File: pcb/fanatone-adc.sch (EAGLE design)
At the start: 43 parts, among them IC2 DIT4192-H, IC3 PCM4201-TSSOP-16, Q1 SST5484, U1 OPA1612AID, U2 TPS62240DRVTG4

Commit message: add datasheets, remove capacitor over R6 at booster
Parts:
- removed C21: 4.7pF, rcl:C-EUC0603
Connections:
- removed net 4V: C10.1, C3.1
- new net 5V: C11.2, C12.2, IC3.VCC
- new net N$12: IC2.SCLK, IC3.BCK
- new net N$14: IC2.SYNC, IC3.FSYNC
- new net N$15: IC2.SDATA, IC3.DATA
- new net N$17: IC2.MCLK, IC3.SCKI
- net 3V3: now also IC3.VDD
- net GND: now also C10.1, C3.1, IC3.DGND, IC3.RATE, IC3.S/M, IC3.VREF-; no longer C10.2, C3.2
- net N$5: now also C10.2, C3.2, IC3.VREF+; no longer C11.2, C12.2
- net N$7: no longer C21.2
- net VCAPSULE: no longer C21.1
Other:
- note added: "24.576 MHz"
- note added: "RATE pin level LOW - high performance, double speed, 96kHz HIGH - low power, 48kHz FLOAT - high performance, 48 kHz"
- note added: "VDPP input 9.5...12.5V"
- note added: "differential input max 5Vp-p 15k input impedance per pin"
- note added: "set R5, R6 for output voltage VCAPSULE = 48V"
- moved on the sheet: C10, C11, C12, C13, C14, C3, C6, C7, C8, D1, R1

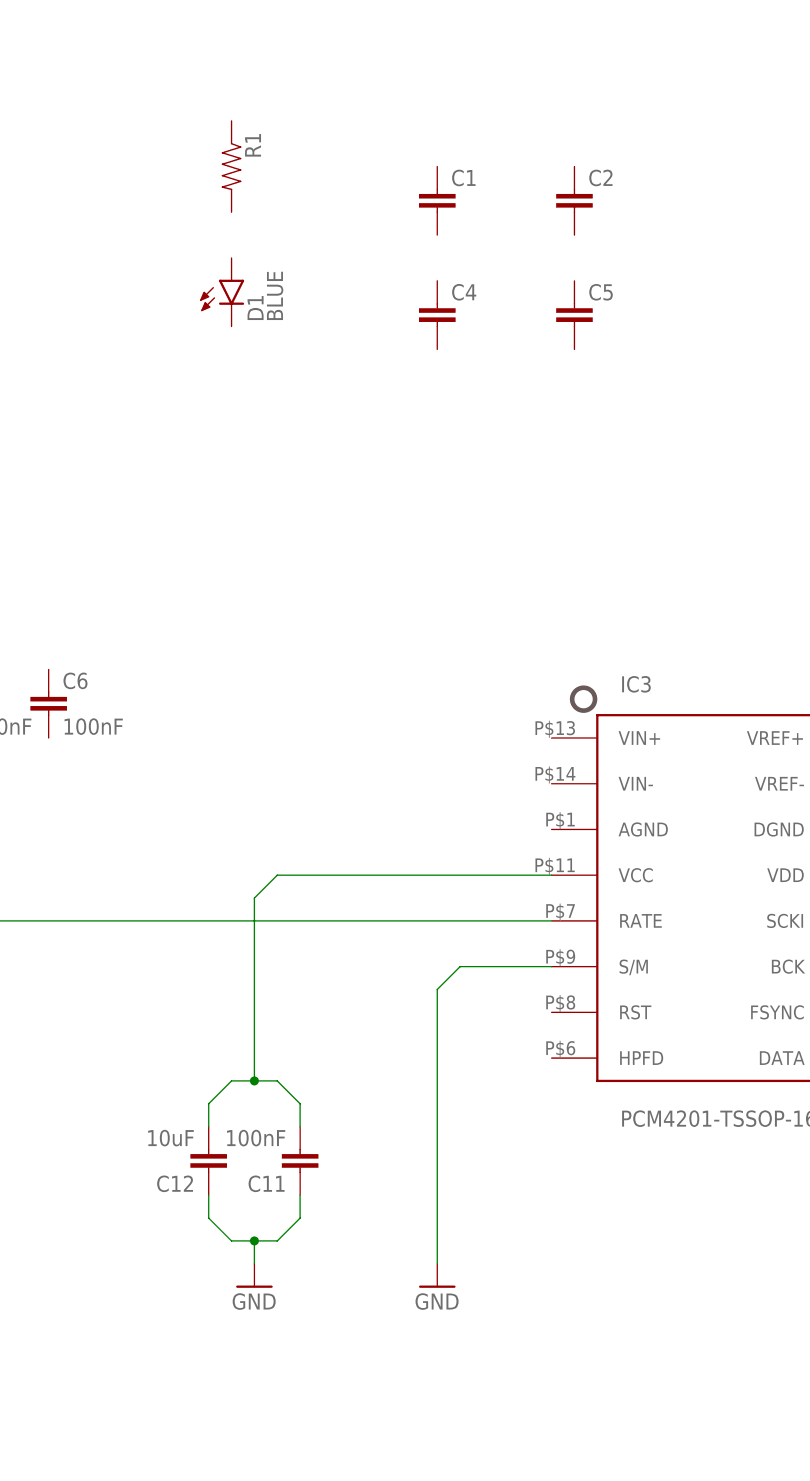
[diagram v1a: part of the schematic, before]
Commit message: Rectangular FAT Capsule R design
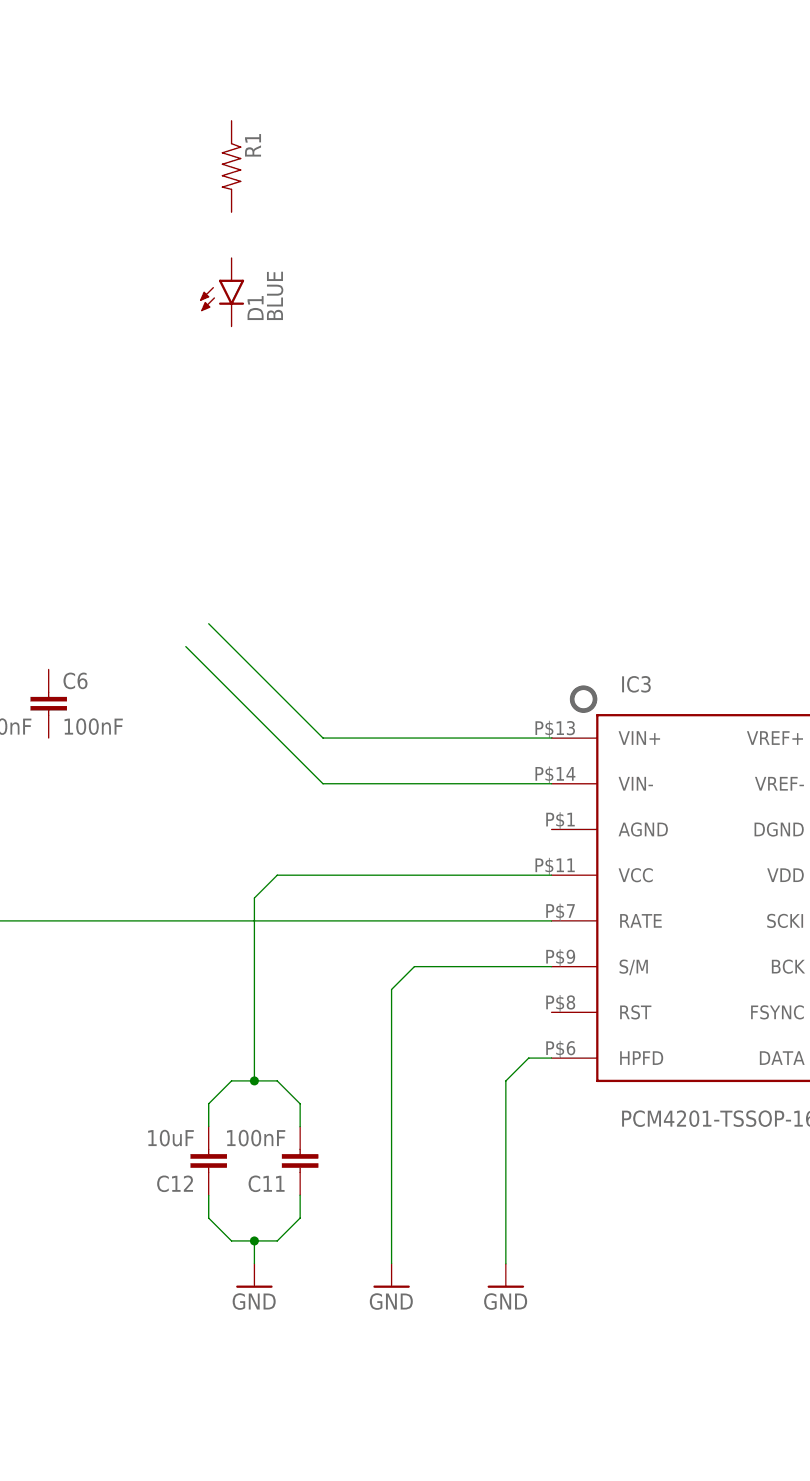
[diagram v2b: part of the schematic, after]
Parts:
- removed C1: (no value), rcl:C-EUC0402K
- removed C2: (no value), rcl:C-EUC0805
- removed C4: (no value), SparkFun-Passives:CAP0603-CAP
- removed C5: (no value), SparkFun-Passives:CAP0805
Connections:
- new net N$19: IC3.VIN+
- new net N$20: IC3.VIN-
- net GND: now also IC3.HPFD
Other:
- note added: "HPFD LOW - enable high pass at 2Hz (-3dB) HIGH - disable (no DC decoupling)"
- note added: "S/M LOW - master"
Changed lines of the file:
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@@
 <part name="FRAME1" library="frames" deviceset="A3L-LOC" device=""/>
 <part name="FRAME2" library="frames" deviceset="A3L-LOC" device=""/>
-<part name="C1" library="rcl" deviceset="C-EU" device="C0402K"/>
-<part name="C2" library="rcl" deviceset="C-EU" device="C0805"/>
 <part name="IC2" library="texas" deviceset="DIT4192-H" device=""/>
 <part name="U$1" library="SparkFun-FreqCtrl" deviceset="CRYSTAL-GROUNDED" device=""/>
-<part name="C4" library="SparkFun-Passives" deviceset="CAP" device="0603-CAP"/>
-<part name="C5" library="SparkFun-Passives" deviceset="CAP" device="0805"/>
 <part name="R1" library="SparkFun-Passives" deviceset="RESISTOR" device="0603-RES"/>
 <part name="D1" library="SparkFun-LED" deviceset="LED-BLUE" device="0603" value="BLUE"/>
@@
 <part name="GND2" library="SparkFun-Aesthetics" deviceset="GND" device=""/>
 <part name="GND16" library="SparkFun-Aesthetics" deviceset="GND" device=""/>
+<part name="GND17" library="SparkFun-Aesthetics" deviceset="GND" device=""/>
 </parts>
 <sheets>
@@
 <text x="312.42" y="142.24" size="1.778" layer="91">9.5 ... 12.5V - Vdrop_D3
 max. 250mA</text>
-<text x="81.28" y="132.08" size="1.778" layer="98">differential input
+<text x="58.42" y="134.62" size="1.778" layer="98">differential input
 max 5Vp-p
 15k input impedance per pin</text>
@@
 <text x="154.94" y="-185.42" size="1.778" layer="98">set R5, R6 for output voltage
 VCAPSULE = 48V</text>
+<text x="81.28" y="66.04" size="1.778" layer="98">HPFD
+LOW - enable high pass at 2Hz (-3dB)
+HIGH - disable (no DC decoupling)</text>
+<text x="65.278" y="66.548" size="1.778" layer="98" rot="R90">S/M
+LOW - master</text>
 </plain>
 <instances>
@@
 <instance part="FRAME1" gate="G$1" x="-7.62" y="-10.16"/>
 <instance part="FRAME2" gate="G$1" x="419.1" y="-10.16"/>
-<instance part="C1" gate="G$1" x="71.12" y="185.42"/>
-<instance part="C2" gate="G$1" x="86.36" y="185.42"/>
 <instance part="IC2" gate="G$1" x="238.76" y="106.68"/>
 <instance part="U$1" gate="G$1" x="190.5" y="182.88"/>
-<instance part="C4" gate="G$1" x="71.12" y="170.18"/>
-<instance part="C5" gate="G$1" x="86.36" y="170.18"/>
 <instance part="R1" gate="G$1" x="48.26" y="187.96" rot="R270"/>
 <instance part="D1" gate="G$1" x="48.26" y="175.26"/>
@@
 <instance part="U1" gate="A" x="604.52" y="193.04"/>
 <instance part="IC3" gate="G$1" x="101.6" y="106.68"/>
-<instance part="GND14" gate="1" x="71.12" y="63.5"/>
+<instance part="GND14" gate="1" x="66.04" y="63.5"/>
 <instance part="GND15" gate="1" x="50.8" y="63.5"/>
 <instance part="C3" gate="G$1" x="187.96" y="78.74" rot="R180"/>
@@
 <instance part="GND2" gate="1" x="182.88" y="63.5"/>
 <instance part="GND16" gate="1" x="7.62" y="63.5"/>
+<instance part="GND17" gate="1" x="78.74" y="63.5"/>
 </instances>
 <busses>
@@
 <segment>
 <pinref part="IC3" gate="G$1" pin="S/M"/>
-<wire x1="83.82" y1="99.06" x2="73.66" y2="99.06" width="0.1524" layer="91"/>
-<wire x1="73.66" y1="99.06" x2="71.12" y2="96.52" width="0.1524" layer="91"/>
-<wire x1="71.12" y1="96.52" x2="71.12" y2="66.04" width="0.1524" layer="91"/>
+<wire x1="83.82" y1="99.06" x2="68.58" y2="99.06" width="0.1524" layer="91"/>
+<wire x1="68.58" y1="99.06" x2="66.04" y2="96.52" width="0.1524" layer="91"/>
+<wire x1="66.04" y1="96.52" x2="66.04" y2="66.04" width="0.1524" layer="91"/>
 <pinref part="GND14" gate="1" pin="GND"/>
 </segment>
@@
 <wire x1="5.08" y1="119.38" x2="2.54" y2="116.84" width="0.1524" layer="91"/>
 <wire x1="2.54" y1="106.68" x2="2.54" y2="116.84" width="0.1524" layer="91"/>
+</segment>
+<segment>
+<pinref part="IC3" gate="G$1" pin="HPFD"/>
+<wire x1="83.82" y1="88.9" x2="81.28" y2="88.9" width="0.1524" layer="91"/>
+<wire x1="81.28" y1="88.9" x2="78.74" y2="86.36" width="0.1524" layer="91"/>
+<wire x1="78.74" y1="86.36" x2="78.74" y2="66.04" width="0.1524" layer="91"/>
+<pinref part="GND17" gate="1" pin="GND"/>
 </segment>
 </net>
@@
 </segment>
 </net>
+<net name="N$19" class="0">
+<segment>
+<pinref part="IC3" gate="G$1" pin="VIN+"/>
+<wire x1="83.82" y1="124.46" x2="58.42" y2="124.46" width="0.1524" layer="91"/>
+<wire x1="58.42" y1="124.46" x2="45.72" y2="137.16" width="0.1524" layer="91"/>
+</segment>
+</net>
+<net name="N$20" class="0">
+<segment>
+<pinref part="IC3" gate="G$1" pin="VIN-"/>
+<wire x1="83.82" y1="119.38" x2="58.42" y2="119.38" width="0.1524" layer="91"/>
+<wire x1="58.42" y1="119.38" x2="43.18" y2="134.62" width="0.1524" layer="91"/>
+</segment>
+</net>

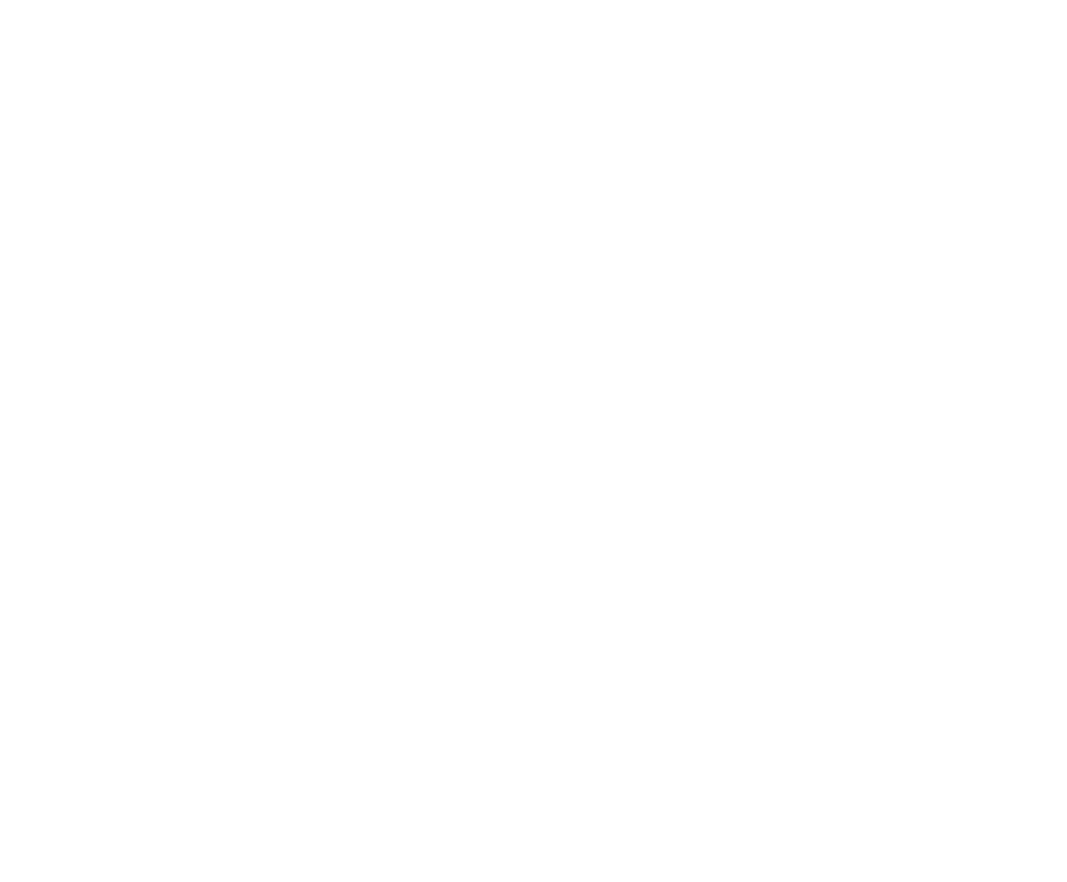
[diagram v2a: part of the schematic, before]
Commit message: start with OPA2134 at the initial gain stage
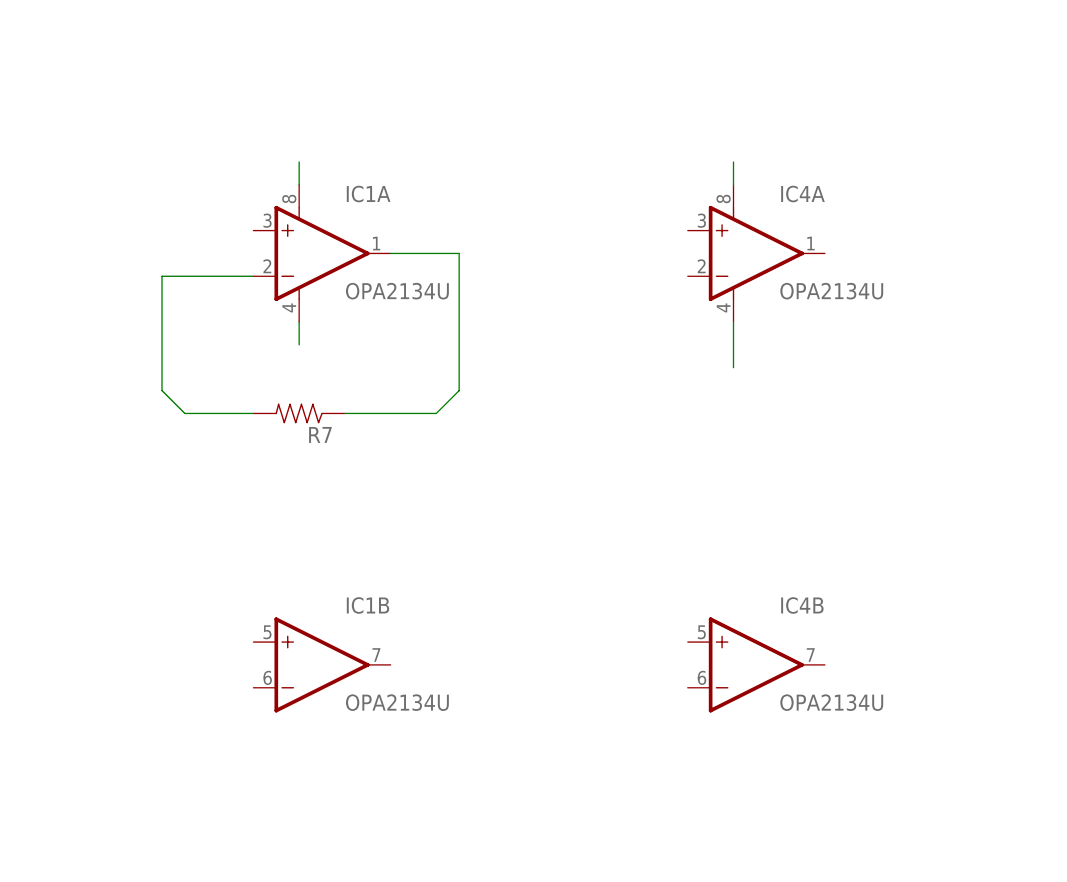
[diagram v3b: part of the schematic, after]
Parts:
- added IC1, IC4: OPA2134U, burr-brown:OPA2134U
- added R7: (no value), SparkFun-Passives:RESISTOR0603-RES
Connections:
- new net N$21: IC1A.OUT, R7.1
- new net N$22: IC1A.-IN, R7.2
- new net N$23: IC1A.V-
- new net N$24: IC1A.V+
- new net N$25: IC4A.V+
- new net N$26: IC4A.V-
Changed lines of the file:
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@@
 <part name="GND16" library="SparkFun-Aesthetics" deviceset="GND" device=""/>
 <part name="GND17" library="SparkFun-Aesthetics" deviceset="GND" device=""/>
+<part name="IC1" library="burr-brown" deviceset="OPA2134" device="U"/>
+<part name="IC4" library="burr-brown" deviceset="OPA2134" device="U"/>
+<part name="R7" library="SparkFun-Passives" deviceset="RESISTOR" device="0603-RES"/>
 </parts>
 <sheets>
@@
 <instance part="GND16" gate="1" x="7.62" y="63.5"/>
 <instance part="GND17" gate="1" x="78.74" y="63.5"/>
+<instance part="IC1" gate="A" x="510.54" y="96.52"/>
+<instance part="IC1" gate="B" x="510.54" y="50.8"/>
+<instance part="IC4" gate="A" x="558.8" y="96.52"/>
+<instance part="IC4" gate="B" x="558.8" y="50.8"/>
+<instance part="R7" gate="G$1" x="508" y="78.74" rot="R180"/>
 </instances>
 <busses>
@@
 </segment>
 </net>
+<net name="N$21" class="0">
+<segment>
+<pinref part="R7" gate="G$1" pin="1"/>
+<wire x1="513.08" y1="78.74" x2="523.24" y2="78.74" width="0.1524" layer="91"/>
+<wire x1="523.24" y1="78.74" x2="525.78" y2="81.28" width="0.1524" layer="91"/>
+<wire x1="525.78" y1="81.28" x2="525.78" y2="96.52" width="0.1524" layer="91"/>
+<pinref part="IC1" gate="A" pin="OUT"/>
+<wire x1="525.78" y1="96.52" x2="518.16" y2="96.52" width="0.1524" layer="91"/>
+</segment>
+</net>
+<net name="N$22" class="0">
+<segment>
+<pinref part="IC1" gate="A" pin="-IN"/>
+<wire x1="502.92" y1="93.98" x2="492.76" y2="93.98" width="0.1524" layer="91"/>
+<wire x1="492.76" y1="93.98" x2="492.76" y2="81.28" width="0.1524" layer="91"/>
+<wire x1="492.76" y1="81.28" x2="495.3" y2="78.74" width="0.1524" layer="91"/>
+<pinref part="R7" gate="G$1" pin="2"/>
+<wire x1="495.3" y1="78.74" x2="502.92" y2="78.74" width="0.1524" layer="91"/>
+</segment>
+</net>
+<net name="N$23" class="0">
+<segment>
+<pinref part="IC1" gate="A" pin="V-"/>
+<wire x1="508" y1="88.9" x2="508" y2="86.36" width="0.1524" layer="91"/>
+</segment>
+</net>
+<net name="N$24" class="0">
+<segment>
+<pinref part="IC1" gate="A" pin="V+"/>
+<wire x1="508" y1="104.14" x2="508" y2="106.68" width="0.1524" layer="91"/>
+</segment>
+</net>
+<net name="N$25" class="0">
+<segment>
+<pinref part="IC4" gate="A" pin="V+"/>
+<wire x1="556.26" y1="104.14" x2="556.26" y2="106.68" width="0.1524" layer="91"/>
+</segment>
+</net>
+<net name="N$26" class="0">
+<segment>
+<pinref part="IC4" gate="A" pin="V-"/>
+<wire x1="556.26" y1="88.9" x2="556.26" y2="83.82" width="0.1524" layer="91"/>
+</segment>
+</net>
